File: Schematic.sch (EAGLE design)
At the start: 48 parts, among them IC2 LM358N, Q1 IRF3205, Q2 IRF3205, Q3 IRF3205, Q4 IRF3205, X1 12Vcc IN, X2 MOTOR DC

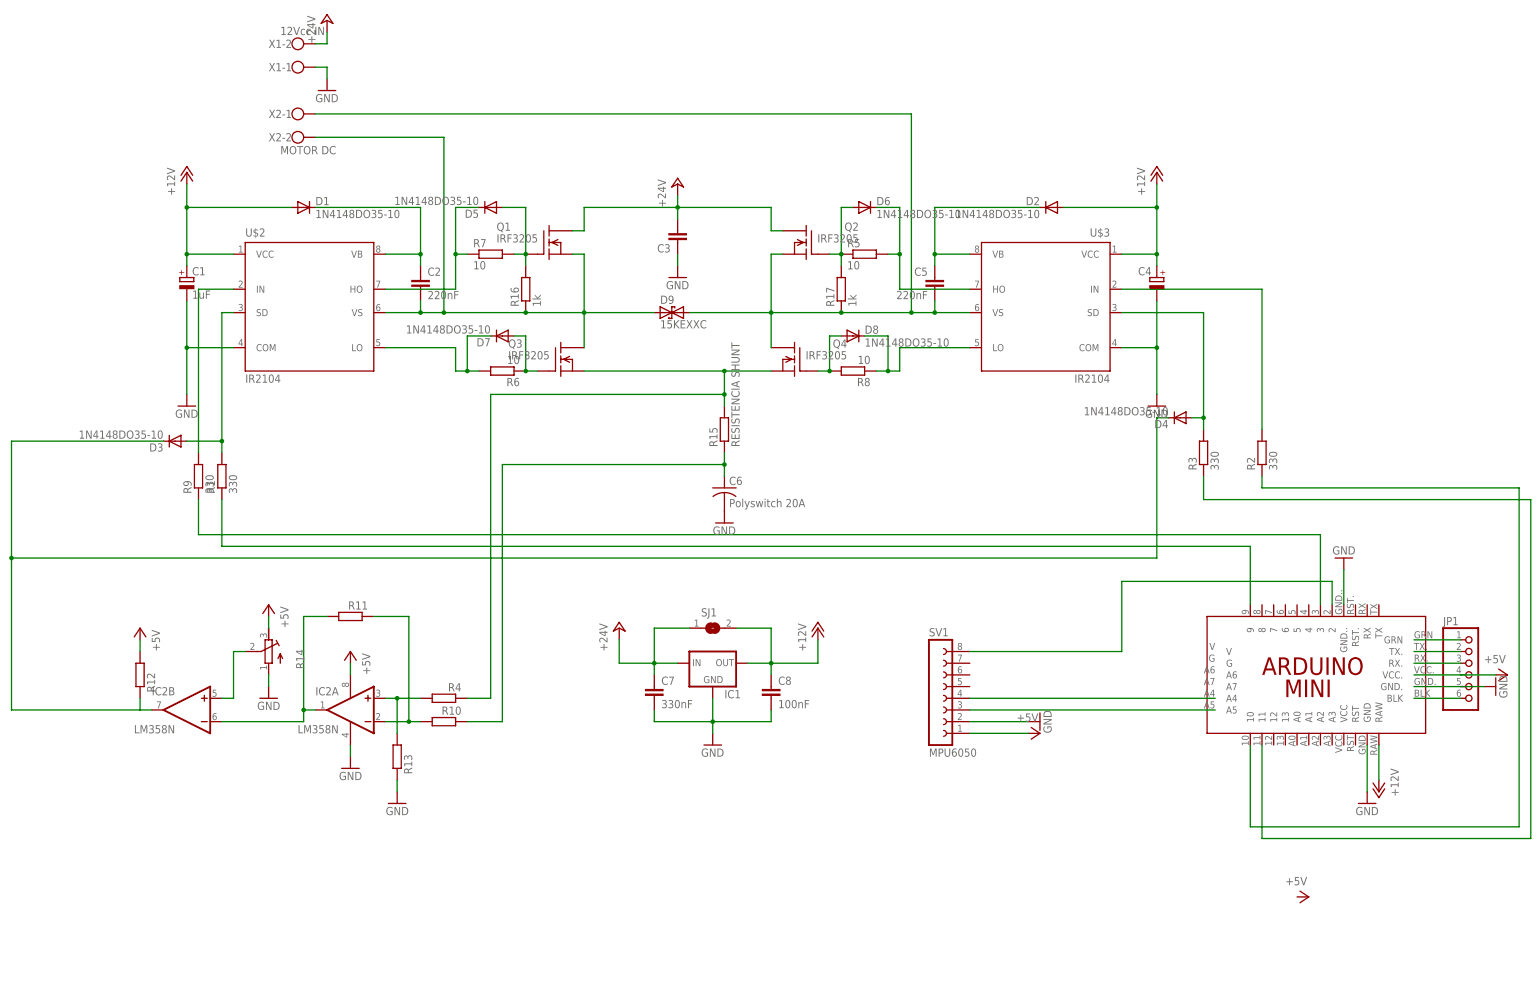
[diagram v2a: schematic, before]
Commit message: Ver 4
Board: I made a mistake and the mosfets weren't as robust as the motor require, so i put two in parallel by vertex of the H bridge (8 in total ).
Algorithm: Some adjustments at parameters.
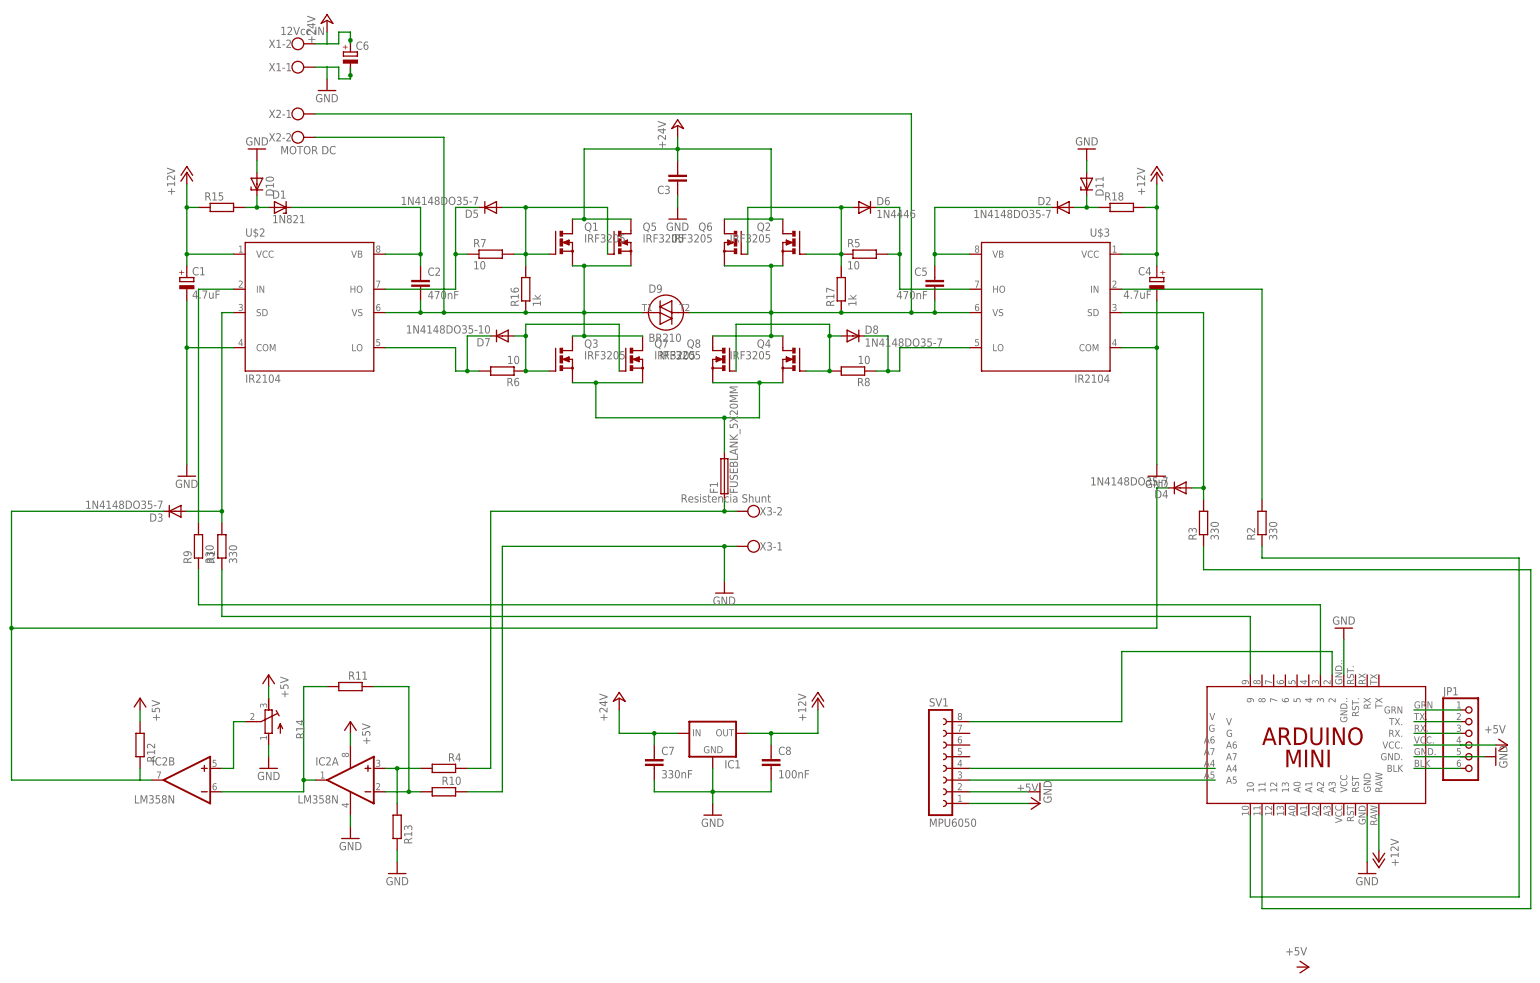
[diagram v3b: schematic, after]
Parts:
- removed SJ1: (no value), jumper:SJW
- added D10, D11: (no value), diode Victor:ZENER-DIODEDO34-7
- added F1: FUSEBLANK_5X20MM, fuse:FUSEBLANK_5X20MM
- added Q5, Q6, Q7, Q8: IRF3205, transistor-power:PMOSFET_NTO220BV
- added R18: (no value), rcl_Victor:R-EU_0204/7
- added X3: Resistencia Shunt, con-wago-500:W237-102
- C1: value 1uF -> 4.7uF
- C2, C5: value 220nF -> 470nF
- C4: value (none) -> 4.7uF
- C6: value Polyswitch 20A -> (none); device rcl:C-US075-032X103 -> rcl_Victor:CPOL-EUE5-13
- D1: value 1N4148DO35-10 -> 1N821; device diode:1N4148DO35-10 -> diode:1N821
- D2, D3, D4, D8: value 1N4148DO35-10 -> 1N4148DO35-7; device diode:1N4148DO35-10 -> diode:1N4148DO35-7
- D5: value 1N4148DO35-10 -> 1N4148DO35-7; device diode:1N4148DO35-10 -> diode Victor:1N4148DO35-7
- D6: value 1N4148DO35-10 -> 1N4446; device diode:1N4148DO35-10 -> diode:1N4446
- D9: value 15KEXXC -> BR210; device diode:15KEXXC -> diode:BR210
- Q1, Q2, Q3, Q4: device transistor-fet Victor:BUZ10 -> transistor-power:PMOSFET_NTO220BV
- R15: value RESISTENCIA SHUNT -> (none); device resistor:R-EU_0922V -> rcl_Victor:R-EU_0204/7
- R16, R9: device rcl:R-EU_0207/10 -> rcl_Victor:R-EU_0207/10
- R17, R7: device rcl:R-EU_0207/10 -> rcl_Victor:R-EU_0204/7
- R2, R3: device rcl:R-EU_0204/7 -> rcl_Victor:R-EU_0207/12
- R5: device rcl:R-EU_0207/12 -> rcl_Victor:R-EU_0207/12
- R6: device rcl:R-EU_0207/10 -> rcl_Victor:R-EU_0207/12
- R8: device rcl:R-EU_0207/15 -> rcl_Victor:R-EU_0204/7
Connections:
- removed net N$34: C6.1, R10.1, R15.1
- new net N$14: D5.A, Q1.G, Q5.G, R16.2, R7.2
- new net N$17: D1.A, D10.C, R15.2
- new net N$29: D11.C, D2.A, R18.1
- net +12V: now also R15.1, R18.2; no longer D1.A, D2.A, SJ1.2
- net +24V: now also C6.+, Q5.D, Q6.D; no longer SJ1.1
- net GND: now also C6.-, D10.A, D11.A, R10.1, X3-1.KL; no longer C6.2
- net N$11: now also Q8.G
- net N$13: now also D9.T1, Q5.S, Q7.D; no longer D9.1
- net N$16: now also D9.T2, Q6.S, Q8.D; no longer D9.2
- net N$18: now also F1.2, Q7.S, Q8.S; no longer R15.2, R4.1
- net N$3: now also F1.1, R4.1, X3-2.KL; no longer D5.A, Q1.G, R16.2, R7.2
- net N$4: now also Q6.G
- net N$9: now also Q7.G
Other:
- moved on the sheet: C3, C7, C8, D2, D3, D4, IC1, IC2A, IC2B, JP1, R1, R10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

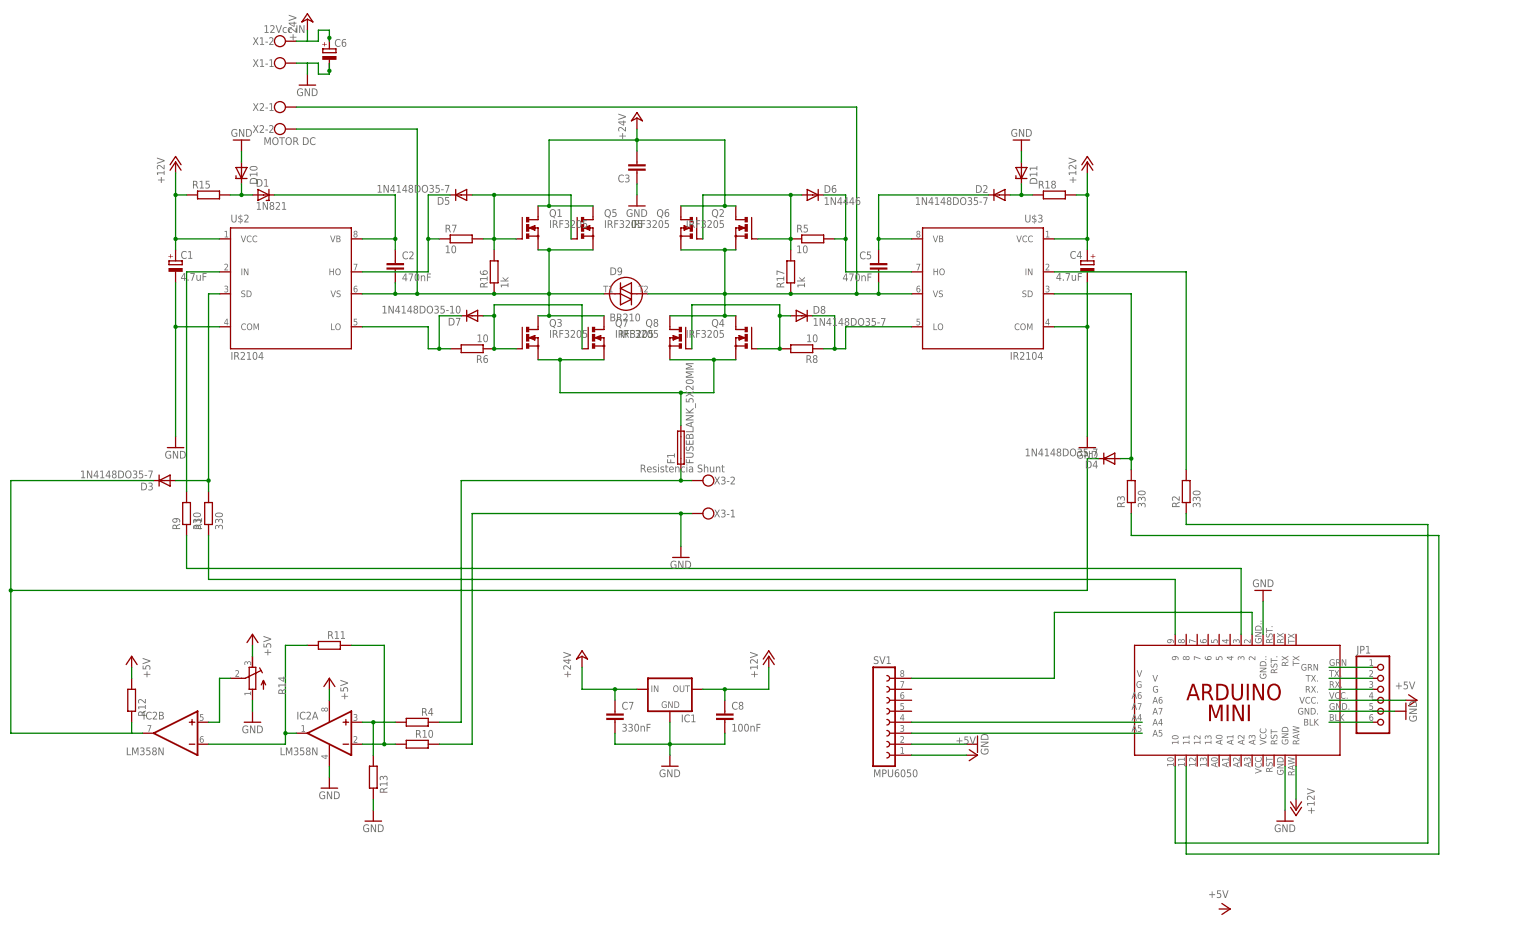
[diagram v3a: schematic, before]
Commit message: Ver 5
Board: The power consumption is huge, so i needed to make thicker the board contacts. I also included a battery charge sensing.
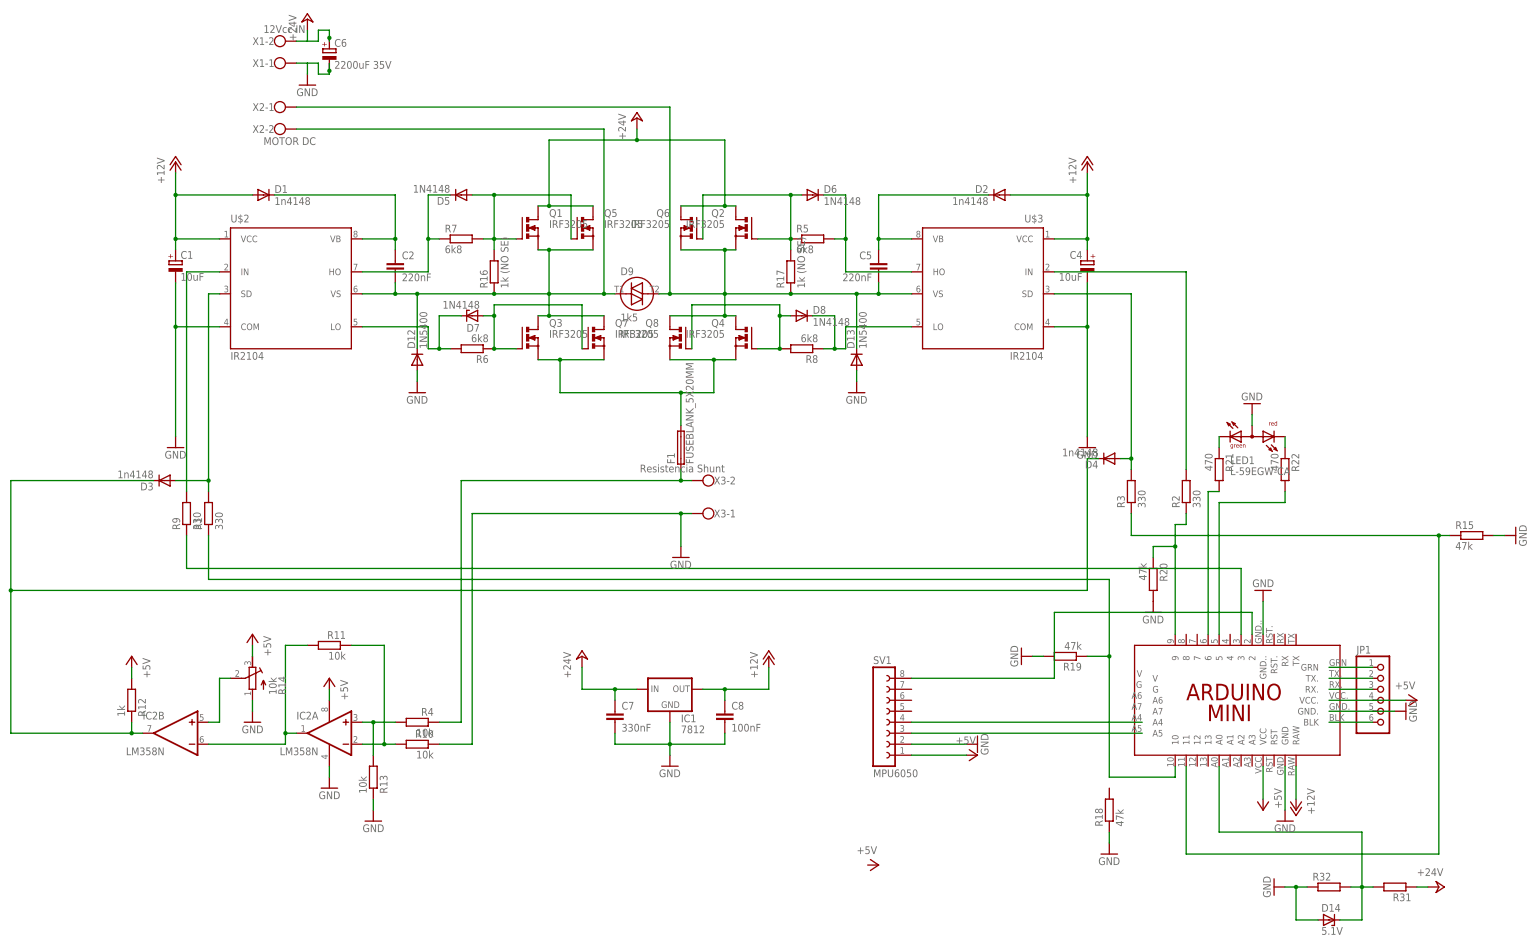
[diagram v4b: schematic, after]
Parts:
- removed C3: (no value), rcl:C-EU050-030X075
- removed D10, D11: (no value), diode Victor:ZENER-DIODEDO34-7
- added D12, D13: 1N5400, diode Victor:1N5400
- added D14: 5.1V, diode Victor:ZENER-DIODEDO34-7
- added LED1: L-59EGW-CA, led:L-59EGW-CA
- added R19, R20: 47k, rcl:R-EU_0204/5
- added R21, R22: 470, rcl:R-EU_0204/5
- added R31, R32: (no value), rcl:R-EU_0204/5
- C1, C4: value 4.7uF -> 10uF
- C2, C5: value 470nF -> 220nF; device rcl:C-EU075-032X103 -> rcl:C-EU050-024X044
- C6: value (none) -> 2200uF 35V
- D1: value 1N821 -> 1n4148; device diode:1N821 -> diode:1N4446
- D2, D3, D4: value 1N4148DO35-7 -> 1n4148
- D5, D8: value 1N4148DO35-7 -> 1N4148
- D6: value 1N4446 -> 1N4148
- D7: value 1N4148DO35-10 -> 1N4148; device diode:1N4148DO35-10 -> diode:1N821
- D9: value BR210 -> 1k5
- IC1: value (none) -> 7812
- R10, R11, R13, R14, R4: value (none) -> 10k
- R12: value (none) -> 1k
- R15, R18: value (none) -> 47k; device rcl_Victor:R-EU_0204/7 -> rcl:R-EU_0204/5
- R16: value 1k -> 1k (NO SE)
- R17: value 1k -> 1k (NO SE); device rcl_Victor:R-EU_0204/7 -> rcl_Victor:R-EU_0207/10
- R5, R7, R8: value 10 -> 6k8
- R6: value 10 -> 6k8; device rcl_Victor:R-EU_0207/12 -> rcl_Victor:R-EU_0207/15
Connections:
- new net N$30: LED1.CG, R21.1
- new net N$34: C5.2, D13.C, D9.T2, Q2.S, Q4.D, Q6.S, Q8.D, R17.1, U$3.VS, X2-1.KL
- new net N$61: D14.C, R31.2, R32.2, U$1.A0
- net +12V: now also D1.A, D2.A; no longer R15.1, R18.2
- net +24V: now also R31.1; no longer C3.2
- net +5V: now also U$1.VCC
- net GND: now also D12.A, D13.A, D14.A, LED1.A, R15.2, R18.1, R19.2, R20.2, R32.1; no longer C3.1, D10.A, D11.A
- net N$13: now also D12.C
- net N$16: now also LED1.CR, R22.1; no longer C5.2, D9.T2, Q2.S, Q4.D, Q6.S, Q8.D, R17.1, U$3.VS, X2-1.KL
- net N$17: now also R21.2, U$1.6; no longer D1.A, D10.C, R15.2
- net N$19: now also R22.2, U$1.5; no longer R2.1, U$1.10
- net N$29: now also R2.1, R20.1, U$1.9; no longer D11.C, D2.A, R18.1
- net N$33: now also R15.1
- net N$7: now also R19.1, U$1.10; no longer U$1.9
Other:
- moved on the sheet: D9, R15, R18
